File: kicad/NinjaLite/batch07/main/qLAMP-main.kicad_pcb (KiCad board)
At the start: 2 copper layers, 142 x 58 mm, 98 parts, among them J1 ALI_USB, J13 Conn_01x01_Male, J16 Conn_01x01_Male, J2 Barrel_Jack_Switch, J24 Conn_01x02_Male, J25 Conn_01x02_Male, J3 Conn_01x07_Male, J4 Conn_01x02_Male, J5 Conn_01x14_Male, J6 Conn_01x01_Male, J7 Conn_01x04_Male, Q1 Q_NMOS_GSD, Q3 Q_NMOS_GSD, Q5 Q_NMOS_GSD, U1 NAU7802, U10 TLC5929, U11 IP2721, U12 ESP32-­S3-­WROOM­-1, U14 TCR3DF33,LM(CT, U19 CD74HC4067M96, U2 NAU7802, U3 BD433M5FP-CE2, U4 LMP7717MF_NOPB, U6 BA178M05FP-E2, U7 BD433M5FP-CE2, U8 TS12A12511DCNR, U9 SN74LV4051A

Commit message: sync
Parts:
- added J8: Conn_01x07_Male, Pin_Headers:Pin_Header_Straight_1x07_Pitch2.54mm, F.Cu at (166.6, 123.7)
- J5: value Conn_01x14_Male -> Conn_01x07_Male; footprint Pin_Headers:Pin_Header_Straight_1x14_Pitch2.54mm -> Pin_Headers:Pin_Header_Straight_1x07_Pitch2.54mm
- moved J7 69.4 mm to (171.8, 129.2), turned to 90 degrees
- moved J5 47.8 mm to (166.4, 126.2), turned to 90 degrees
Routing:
- net GNDD: vias 229 -> 227
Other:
- board size 142 x 58 mm -> 156.5 x 138 mm
- board text added: "Diff from batch06/main: 1. Change EdgeCuts to 3d print enclosure 2. Add pins for 2.4inch LCD MSP2402 3. X+14.5mm 4. Change 1.27mm 2x5 sockets to SMT"
- board text removed: "Diff from batch06/main: 1. Change EdgeCuts to 3d print enclosure 2. Add pins for 2.4inch LCD MSP2402"

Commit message: wiring batch7
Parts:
- removed R23: 100k, Resistor_SMD:R_0603_1608Metric
- added J10: Conn_01x08_Pin, Connector_PinHeader_2.54mm:PinHeader_2x04_P2.54mm_Vertical, F.Cu at (236.6, 74.6)
- added J9: Conn_01x02_Pin, Connector_PinHeader_2.54mm:PinHeader_1x02_P2.54mm_Vertical, F.Cu at (213.0, 53.3)
- added R12: 100k, Resistor_SMD:R_0603_1608Metric, F.Cu at (200.1, 56.9)
- added SW1: TACTILE_4, Ninja:SW_TH_Tactile_alps_SKHHLPA010, F.Cu at (238.2, 35.9)
- C23: footprint Ninja-qPCR:35TZV100M6.3X8 -> Ninja:35TZV100M6.3X8
- D10A1, D11A1, D12A1, D13A1, D14A1, D15A1, D16A1, D1A1, D2A1, D3A1, D4A1, D5A1, D6A1, D7A1, D8A1, D9A1: footprint Ninja-qPCR:SFH2200_2201_2240 -> Ninja:SFH2200_2201_2240
- HLID1, HWELL1: footprint Ninja-qPCR:TB_SeeedOPL_320110028 -> Ninja:TB_SeeedOPL_320110028
- J1: footprint Ninja-qPCR:ALI_USB -> Ninja:ALI_USB
- J5, J8: footprint Pin_Headers:Pin_Header_Straight_1x07_Pitch2.54mm -> Connector_PinHeader_2.54mm:PinHeader_1x07_P2.54mm_Vertical
- J6: value Conn_01x01_Male -> Conn_01x01_Pin; footprint Pin_Headers:Pin_Header_Straight_1x01_Pitch1.27mm -> Connector_PinHeader_2.54mm:PinHeader_1x01_P2.54mm_Vertical; moved to F.Cu
- J7: footprint Pin_Headers:Pin_Header_Straight_1x04_Pitch2.54mm -> Connector_PinHeader_2.54mm:PinHeader_1x04_P2.54mm_Vertical
- JLN1, JLS1: footprint Connector_PinSocket_1.27mm:PinSocket_2x05_P1.27mm_Vertical -> Connector_PinSocket_1.27mm:PinSocket_2x05_P1.27mm_Vertical_SMD
- JP2: moved to F.Cu
- Q1, Q3, Q5: footprint Ninja-qPCR:SOT95P240X112-3N -> Ninja:SOT95P240X112-3N
- TEXT1, TEXT2, TEXT3, TLID1, TWELL1: footprint Pin_Headers:Pin_Header_Straight_1x02_Pitch2.54mm -> Connector_PinHeader_2.54mm:PinHeader_1x02_P2.54mm_Vertical
- U12: footprint Ninja-qPCR:ESP32-S3-WROOM-1 -> Ninja:ESP32-S3-WROOM-1
- U19: footprint Ninja-qPCR:SSOP-24_5.3x8.2mm_P0.65mm-0.83mil -> Ninja:SSOP-24_5.3x8.2mm_P0.65mm-0.83mil
- U3, U6: footprint Ninja-qPCR:REG_TO252-3 -> Ninja:REG_TO252-3
- U7: footprint Ninja-qPCR:REG_TO252-3-INV -> Ninja:REG_TO252-3-INV
- U8: footprint Ninja-qPCR:SOT-23-8-8.3mil -> Ninja:SOT-23-8-8.3mil
- moved U3 121.3 mm to (278.2, 62.6), turned to 0 degrees
- moved U7 117.5 mm to (278.2, 55.1), turned to 0 degrees
- moved C28 112.1 mm to (275.8, 49.9), turned to 0 degrees
- moved C31 111.4 mm to (275.8, 47.7), turned to 0 degrees
- moved R8 110.7 mm to (265.5, 31.7)
- moved R6 110.7 mm to (268.2, 31.7)
- moved J7 106.2 mm to (247.0, 54.2), turned to 0 degrees
- moved R19 102.8 mm to (268.0, 37.4)
- moved R20 102.8 mm to (265.3, 37.4)
- moved J3 100.0 mm to (230.2, 39.5), turned to -90 degrees
- moved U6 96.3 mm to (275.2, 78.9), turned to 0 degrees
- moved JP2 96.3 mm to (223.5, 42.1), turned to -90 degrees
- moved C25 92.4 mm to (256.9, 48.1)
- moved C23 92.4 mm to (263.0, 49.8)
- moved C27 92.4 mm to (255.6, 50.7)
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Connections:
- J3 pad 1: /TACT2 -> /BOOTMODE
- J5 pad 2: /SD_MISO -> /MISO
- J5 pad 3: /SD_MOSI -> MOSI
- J5 pad 5: /SD_CLK -> SCLK
- J5 pad 6: /SD_MISO -> /MISO
- J6 pad 1: Net-(J6-Pad1) -> /IO1
- J8 pad 1: /SD_CLK -> SCLK
- J8 pad 2: /SD_MOSI -> MOSI
- U12 pad 10: /WELL_HEATER -> VIN_SENSE
- U12 pad 11: /LID_HEATER -> /IO18
- U12 pad 12: THERM_R_SWITCH -> /SD_CLK
- U12 pad 13: LED_LAT -> /SD_MISO
- U12 pad 14: I2C_SCL -> /SD_MOSI
- U12 pad 15: unconnected-(U12-Pad15) -> /SD_CS
- U12 pad 16: unconnected-(U12-Pad16) -> /LCD_CS
- U12 pad 17: I2C_SDA -> /LCD_RESET
- U12 pad 19: /LCD_RESET -> /IO11
- U12 pad 20: /LCD_CS -> /IO12
- U12 pad 21: /SD_MOSI -> SCLK
- U12 pad 22: /SD_MISO -> /MISO
- U12 pad 23: /SD_CLK -> MOSI
- U12 pad 24: /SD_CS -> /TP_CS
- U12 pad 25: LED_BLANK -> /TP_IRQ
- U12 pad 26: unconnected-(U12-Pad26) -> LED_LAT
- U12 pad 27: unconnected-(U12-Pad27) -> /BOOTMODE
- U12 pad 28: MUX_S0 -> LED_BLANK
- U12 pad 29: MUX_S3 -> NAU_DRDY
- U12 pad 30: unconnected-(U12-Pad30) -> I2C_SCL
- U12 pad 31: unconnected-(U12-Pad31) -> I2C_SDA
- U12 pad 32: SCLK -> THERM_R_SWITCH
- U12 pad 33: Net-(J6-Pad1) -> MUX_S0
- U12 pad 34: unconnected-(U12-Pad34) -> MUX_S3
- U12 pad 39: MOSI -> /IO1
- U12 pad 4: unconnected-(U12-Pad4) -> /IO4
- U12 pad 5: unconnected-(U12-Pad5) -> /IO5
- U12 pad 6: NAU_DRDY -> /IO6
- U12 pad 7: /SD_CD -> /LID_HEATER
- U12 pad 8: VIN_SENSE -> /WELL_HEATER
- U12 pad 9: unconnected-(U12-Pad9) -> /IO16
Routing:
- net 3V3D: track 268.2 -> 171.7 mm, vias 12 -> 5
- net VCC: track 109.8 -> 30.2 mm
- net /MISO: track 0.00 -> 65.4 mm, vias 0 -> 1
- net 5V: track 230.3 -> 168.2 mm, vias 6 -> 7
- net unconnected-(U12-Pad16): track 58.9 -> 0.00 mm, vias 3 -> 0
- net /TP_CS: track 0.00 -> 48.3 mm, vias 0 -> 1
- net GNDD: track 379.0 -> 331.5 mm, vias 227 -> 82
- net THERM_R_SWITCH: track 111.3 -> 67.6 mm
- net unconnected-(U12-Pad27): track 41.6 -> 0.00 mm, vias 2 -> 0
- net /TP_IRQ: track 0.00 -> 38.3 mm, vias 0 -> 1
- net /LCD_CS: track 0.00 -> 33.9 mm, vias 0 -> 1
- net /LCD_RESET: track 0.00 -> 30.4 mm, vias 0 -> 1
- net MUX_S2: track 197.5 -> 168.1 mm
- net /LCD_DC/RS: track 0.00 -> 28.4 mm, vias 0 -> 1
- net MOSI: track 91.7 -> 118.0 mm, vias 4 -> 3
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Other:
- board size 156.5 x 138 mm -> 190.1 x 58 mm
- board text added: "181.5x58mm"
- board text added: "Diff from batch06/main: 1. Change EdgeCuts to 3d print enclosure 2. Add pins for 2.8inch LCD MSP2402 3. Change 1.27mm 2x5 sockets to SMT"
- board text added: "Y0"
- board text added: "Y0+80"
- board text added: "Y0-1"
- board text added: "Y0-4"
- board text removed: "142x58mm"
- board text removed: "Diff from batch06/main: 1. Change EdgeCuts to 3d print enclosure 2. Add pins for 2.4inch LCD MSP2402 3. X+14.5mm 4. Change 1.27mm 2x5 sockets to SMT"

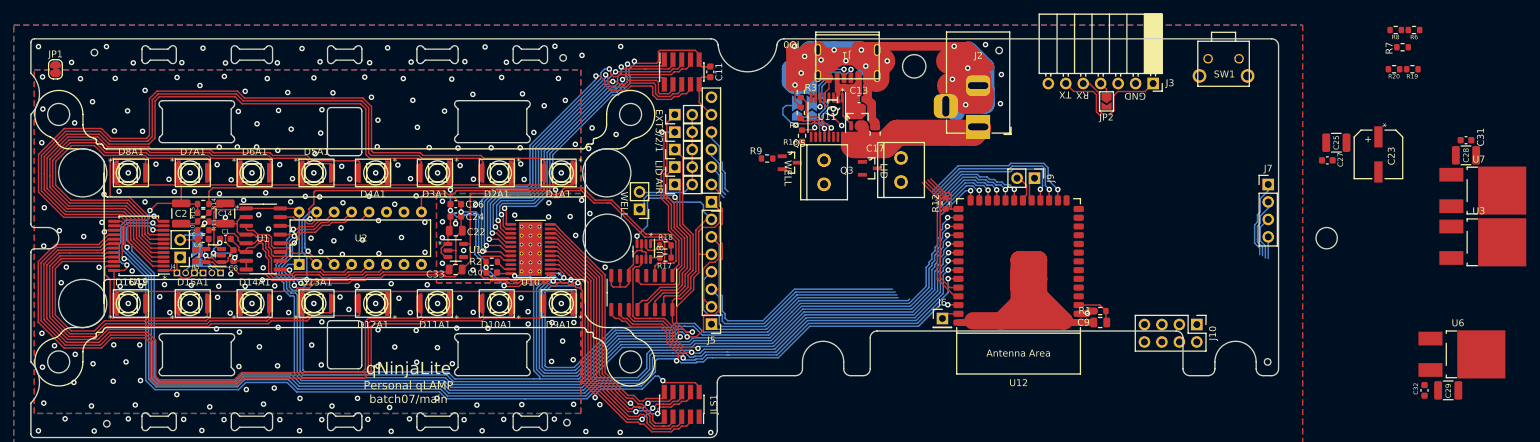
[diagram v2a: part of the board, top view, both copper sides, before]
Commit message: wiring batch7 main
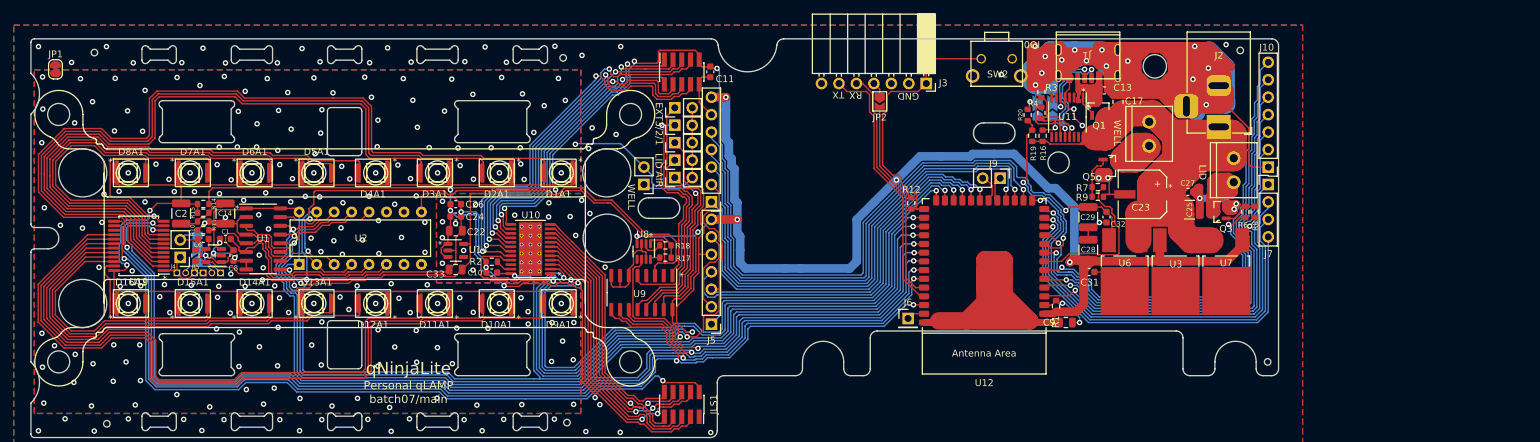
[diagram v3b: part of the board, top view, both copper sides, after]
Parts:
- removed SW1: TACTILE_4, Ninja:SW_TH_Tactile_alps_SKHHLPA010
- added SW2: TACTILE_4, Ninja:SW_TH_Tactile_alps_SKHHLPA010, F.Cu at (205.2, 35.9)
- J10: value Conn_01x08_Pin -> Conn_01x07_Pin; footprint Connector_PinHeader_2.54mm:PinHeader_2x04_P2.54mm_Vertical -> Connector_PinHeader_2.54mm:PinHeader_1x07_P2.54mm_Vertical
- moved C29 58.1 mm to (220.8, 58.9), turned to -90 degrees
- moved C31 58.1 mm to (220.9, 66.9)
- moved C28 56.6 mm to (220.8, 63.7), turned to 90 degrees
- moved R19 56.2 mm to (212.7, 47.1), turned to 90 degrees
- moved R20 53.7 mm to (212.0, 44.1), turned to 90 degrees
- moved C32 52.7 mm to (223.5, 58.9)
- moved Q3 51.2 mm to (239.8, 58.2), turned to 180 degrees
- moved U6 50.5 mm to (226.1, 66.9), turned to -90 degrees
- moved R7 48.8 mm to (222.2, 54.6), turned to 0 degrees
- moved R9 48.4 mm to (222.2, 56.0)
- moved HLID1 48.4 mm to (242.0, 50.4)
- moved HWELL1 47.6 mm to (229.7, 45.1)
- moved Q5 46.7 mm to (224.1, 51.5)
- moved U3 44.9 mm to (233.5, 66.9), turned to -90 degrees
- moved U7 39.1 mm to (240.9, 66.9), turned to -90 degrees
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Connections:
- J10 pad 2: GNDD -> 3V3D
- J10 pad 3: 3V3D -> /IO4
- J10 pad 4: /IO4 -> /IO5
- J10 pad 5: /IO5 -> /IO6
- J10 pad 6: /IO6 -> /IO16
- J10 pad 7: /IO16 -> /IO18
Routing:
- net 3V3D: track 171.7 -> 337.0 mm, vias 5 -> 10
- net GNDD: track 331.5 -> 479.3 mm, vias 82 -> 87
- net VCC: track 30.2 -> 142.6 mm
- net 5V: track 168.2 -> 274.6 mm, vias 7 -> 9
- net /IO18: track 0.00 -> 74.2 mm, vias 0 -> 1
- net /IO16: track 0.00 -> 70.1 mm, vias 0 -> 1
- net /IO6: track 0.00 -> 64.7 mm, vias 0 -> 1
- net /IO5: track 0.00 -> 62.8 mm, vias 0 -> 1
- net /IO4: track 0.00 -> 61.1 mm, vias 0 -> 1
- net /SD_CS: track 11.4 -> 66.8 mm, vias 0 -> 1
- net /SD_MOSI: track 8.78 -> 62.4 mm, vias 0 -> 1
- net /SD_MISO: track 6.40 -> 59.8 mm, vias 0 -> 1
- net /SD_CLK: track 3.15 -> 56.3 mm, vias 0 -> 1
- net /LCD_DC/RS: track 28.4 -> 75.0 mm
- net /LCD_RESET: track 30.4 -> 76.6 mm
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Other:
- board size 190.1 x 58 mm -> 181.5 x 58 mm
- board text added: "U9"
